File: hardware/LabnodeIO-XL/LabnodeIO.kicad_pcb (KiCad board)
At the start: 2 copper layers, 106 parts, among them J1 mc 0.5-2.5, J2 EXT3, U1 PCF8574, U2 PCA9685-TSSOP, U3 LM324, U4 LM324, U5 LM324, U6 LM324

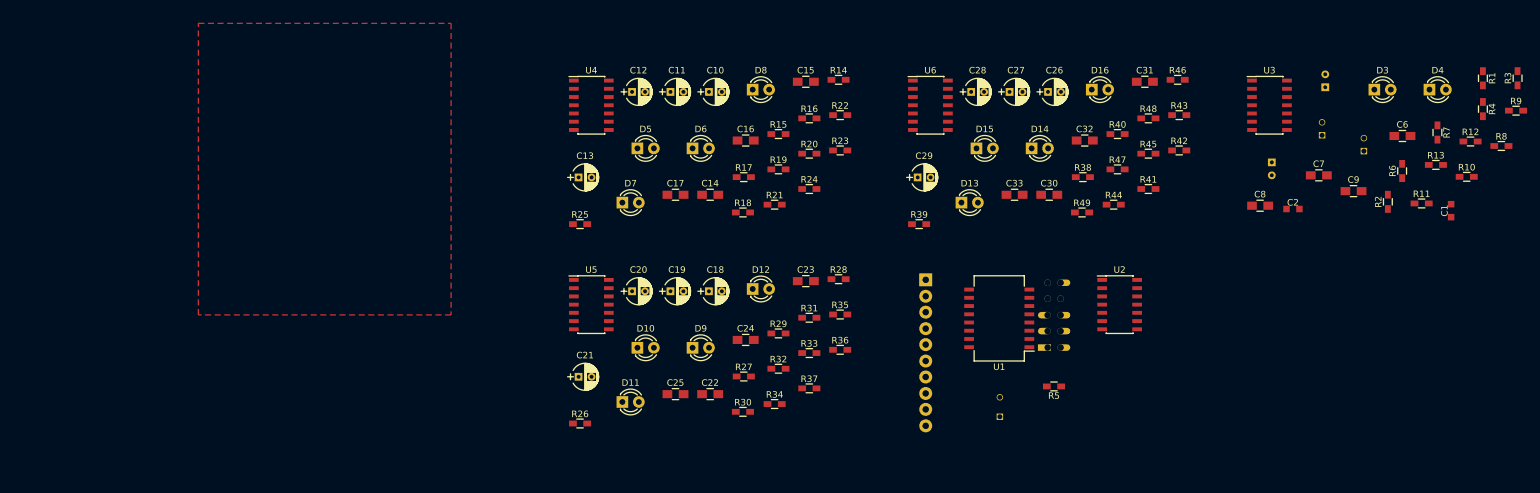
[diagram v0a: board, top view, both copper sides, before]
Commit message: Platinenlayout und 3d modell angefangen
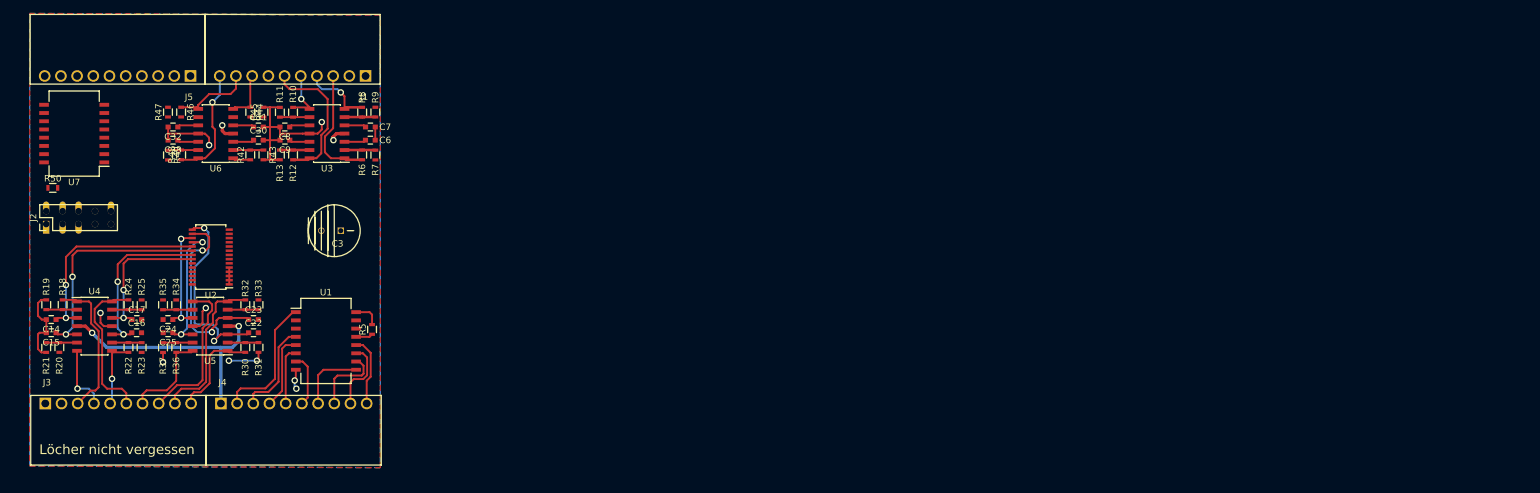
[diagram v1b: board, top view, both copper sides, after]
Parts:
- removed C1, C2: 100u, Capacitors_SMD:C_0805_HandSoldering
- removed C10, C11, C12, C13, C18, C19, C20, C21, C26, C27, C28, C29, C4, C5: 100u, Capacitors_THT:CP_Radial_D4.0mm_P2.00mm
- removed D1, D10, D11, D12, D13, D14, D15, D16, D2, D3, D4, D5, D6, D7, D8, D9: LED_Small, LEDs:LED_D3.0mm
- removed R1, R14, R15, R16, R17, R2, R26, R27, R28, R29, R3, R38, R39, R4, R40, R41: R, Resistors_SMD:R_0603_HandSoldering
- added J3: Conn_01x10, mc-0.5-2:MC-0,5-10-G-2,5, F.Cu at (16.4, 74.2)
- added J4: Conn_01x10, mc-0.5-2:MC-0,5-10-G-2,5, F.Cu at (43.5, 74.2)
- added J5: Conn_01x10, mc-0.5-2:MC-0,5-10-G-2,5, F.Cu at (38.8, 23.6)
- added R50: 1k5, Resistors_SMD:R_0603, F.Cu at (17.5, 40.9)
- added U7: PCF8574, Housings_SOIC:SOIC-16W_7.5x12.8mm_Pitch1.27mm, F.Cu at (20.8, 32.5)
- C14, C15, C16, C17, C22, C23, C24, C25, C30, C31, C32, C33, C6, C7, C8, C9: footprint Capacitors_SMD:C_0805_HandSoldering -> Capacitors_SMD:C_0603
- C3, J2: moved to F.Cu
- J1: value mc 0.5-2.5 -> Conn_01x10; footprint Connectors_Molex:Molex_KK-6410-10_10x2.54mm_Straight -> mc-0.5-2:MC-0,5-10-G-2,5; moved to F.Cu
- R10, R11, R12, R13, R18, R19, R20, R21, R22, R23, R24, R25, R30, R31, R32, R33, R34, R35, R36, R37, R42, R43, R44, R45, R46, R47, R48, R49, R5, R6, R7, R8, R9: footprint Resistors_SMD:R_0603_HandSoldering -> Resistors_SMD:R_0603
- U2: footprint Housings_SOIC:SOIC-14_3.9x8.7mm_Pitch1.27mm -> Housings_SSOP:TSSOP-28_4.4x9.7mm_Pitch0.65mm
- moved R12 181.7 mm to (54.6, 35.8), turned to 90 degrees
- moved R10 181.4 mm to (54.6, 29.2), turned to 270 degrees
- moved R13 178.4 mm to (52.6, 35.8), turned to 270 degrees
- moved R11 176.8 mm to (52.6, 29.2), turned to 90 degrees
- moved R9 176.0 mm to (67.3, 29.2), turned to 90 degrees
- moved R8 175.9 mm to (65.3, 29.2), turned to 270 degrees
- moved C9 165.1 mm to (53.4, 33.5), turned to 180 degrees
- moved R7 164.0 mm to (67.3, 35.8)
- moved R6 160.5 mm to (65.3, 35.8)
- moved C6 159.3 mm to (66.5, 33.5)
- moved J2 155.7 mm to (16.5, 46.5), turned to 90 degrees
- moved R46 153.9 mm to (37.3, 29.2), turned to 270 degrees
- moved C8 151.0 mm to (53.3, 31.5), turned to 180 degrees
- moved R48 149.4 mm to (37.3, 35.8), turned to 90 degrees
- moved R47 146.8 mm to (35.3, 29.2), turned to 90 degrees
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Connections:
- J1 pad 1: Net-(J1-Pad1) -> GND
- J1 pad 10: +12V -> /analog5-8/out4
- J1 pad 2: Net-(J1-Pad2) -> GND
- J1 pad 3: Net-(J1-Pad3) -> /analog1-4/out1
- J1 pad 4: Net-(J1-Pad4) -> /analog1-4/out2
- J1 pad 5: Net-(J1-Pad5) -> /analog1-4/out3
- J1 pad 6: Net-(J1-Pad6) -> /analog1-4/out4
- J1 pad 7: Net-(J1-Pad7) -> /analog5-8/out1
- J1 pad 8: Net-(J1-Pad8) -> /analog5-8/out2
- J1 pad 9: +5V -> /analog5-8/out3
- U1 pad 1: GND -> +5V
- U1 pad 10: Net-(J1-Pad3) -> /digital 1-8/digital6
- U1 pad 11: Net-(J1-Pad2) -> /digital 1-8/digital7
- U1 pad 12: Net-(J1-Pad1) -> /digital 1-8/digital8
- U1 pad 4: Net-(J1-Pad8) -> /digital 1-8/digital1
- U1 pad 5: Net-(J1-Pad7) -> /digital 1-8/digital2
- U1 pad 6: Net-(J1-Pad6) -> /digital 1-8/digital3
- U1 pad 7: Net-(J1-Pad5) -> /digital 1-8/digital4
- U1 pad 9: Net-(J1-Pad4) -> /digital 1-8/digital5
- U2 pad 1: (no net) -> GND
- U2 pad 10: /analog5-8/out1 -> /analog5-8/in1
- U2 pad 11: /analog5-8/out2 -> /analog5-8/in2
- U2 pad 12: /analog5-8/out3 -> /analog5-8/in3
- U2 pad 13: /analog5-8/out4 -> /analog5-8/in4
- U2 pad 2: (no net) -> GND
- U2 pad 3: (no net) -> GND
- U2 pad 4: (no net) -> GND
- U2 pad 5: (no net) -> GND
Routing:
- net GND: track 0.00 -> 76.6 mm, vias 0 -> 9
- net +12V: track 0.00 -> 44.7 mm, vias 0 -> 4
- net /analog9-12/in2: track 0.00 -> 34.7 mm, vias 0 -> 2
- net /analog9-12/in1: track 0.00 -> 32.9 mm, vias 0 -> 2
- net /analog13-16/in2: track 0.00 -> 29.7 mm, vias 0 -> 2
- net /analog13-16/in1: track 0.00 -> 29.6 mm, vias 0 -> 2
- net /analog9-12/in3: track 0.00 -> 26.4 mm, vias 0 -> 2
- net +5V: track 0.00 -> 24.5 mm
- net /analog13-16/out2: track 0.00 -> 24.5 mm
- net /analog9-12/out4: track 0.00 -> 23.8 mm
- net /analog13-16/out3: track 0.00 -> 23.8 mm
- net /analog9-12/out1: track 0.00 -> 22.7 mm
- net /analog9-12/in4: track 0.00 -> 22.5 mm, vias 0 -> 2
- net /analog1-4/out4: track 0.00 -> 22.4 mm
- net /analog13-16/in4: track 0.00 -> 20.9 mm, vias 0 -> 2
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- added copper zone on B.Cu, net GND
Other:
- net class Default: clearance 0.4 -> 0.25; trace_width 0.5 -> 0.3; via_dia 1.5 -> 1; via_drill 1 -> 0.6
- net class POWER added: clearance 0.25, trace_width 0.5, via_dia 1, via_drill 0.6
- rule trace_clearance: 0.4 -> 0.25
- board text added: "Löcher nicht vergessen"

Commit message: pwm chip geroutet
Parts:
- moved C3 23.4 mm to (38.6, 47.5)
- moved U2 15.8 mm to (57.7, 51.3)
- moved R50 7.98 mm to (16.3, 33.0), turned to 270 degrees
- moved C15 3.57 mm to (17.0, 66.8)
- moved C16 3.57 mm to (30.2, 66.8)
- moved C22 3.57 mm to (48.2, 66.8)
- moved C25 3.57 mm to (35.1, 66.8)
- moved R18 3.57 mm to (18.8, 62.5)
- moved R19 3.57 mm to (16.3, 62.5)
- moved R24 3.57 mm to (29.0, 62.5)
- moved R25 3.57 mm to (31.0, 62.5)
- moved R32 3.57 mm to (47.0, 62.5)
- moved R33 3.57 mm to (49.0, 62.5)
- moved R34 3.57 mm to (36.3, 62.5)
- moved R35 3.57 mm to (34.3, 62.5)
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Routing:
- net GND: track 76.6 -> 197.2 mm, vias 9 -> 23
- net /analog5-8/in3: track 3.25 -> 42.3 mm, vias 0 -> 2
- net /analog5-8/in4: track 3.25 -> 36.6 mm, vias 0 -> 2
- net +5V: track 24.5 -> 56.1 mm
- net /analog5-8/in2: track 3.25 -> 32.9 mm, vias 0 -> 2
- net /analog5-8/in1: track 3.25 -> 31.8 mm, vias 0 -> 2
- net +12V: track 44.7 -> 71.7 mm
- net /analog9-12/in3: track 26.4 -> 51.0 mm
- net /analog1-4/in3: track 3.17 -> 26.7 mm, vias 0 -> 2
- net /analog1-4/in2: track 3.35 -> 26.2 mm, vias 0 -> 2
- net /analog5-8/out1: track 2.73 -> 24.5 mm, vias 0 -> 1
- net /analog1-4/in1: track 3.34 -> 24.1 mm, vias 0 -> 2
- net /analog1-4/in4: track 3.15 -> 23.1 mm, vias 0 -> 2
- net /analog9-12/in1: track 32.9 -> 52.5 mm
- net /analog13-16/in3: track 17.1 -> 36.3 mm
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
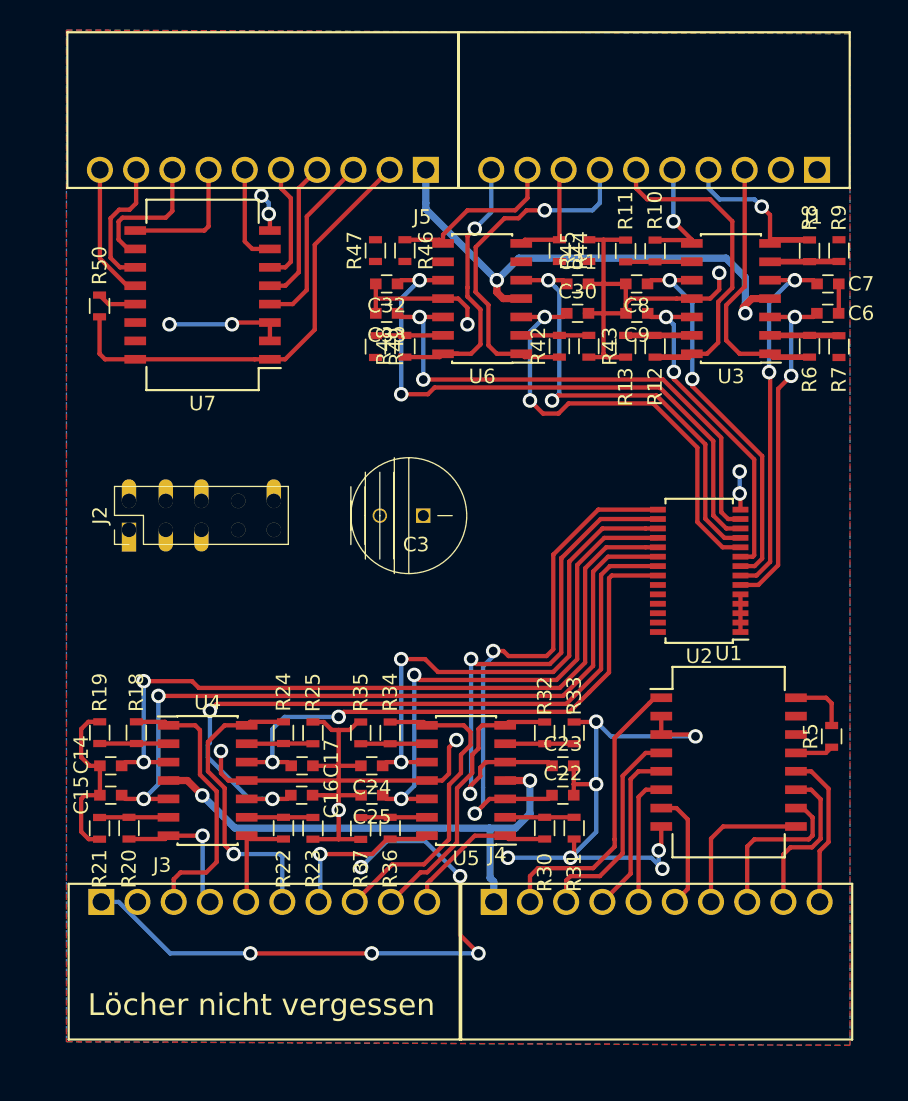
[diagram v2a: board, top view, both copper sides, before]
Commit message: eingangswiderstände hinzugefuegt und geroutet
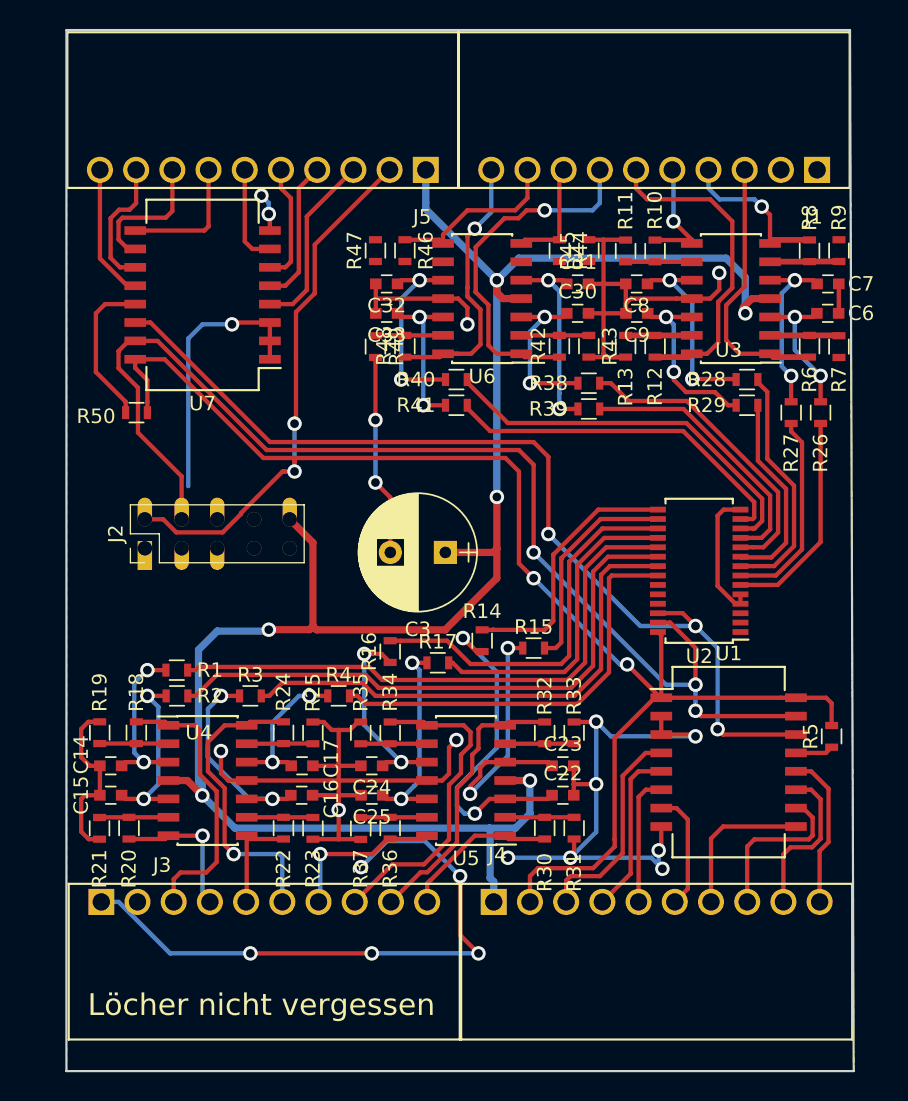
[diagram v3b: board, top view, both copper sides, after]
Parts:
- added R1: 22k, Resistors_SMD:R_0603, F.Cu at (21.6, 58.2)
- added R14: 22k, Resistors_SMD:R_0603, F.Cu at (42.7, 56.1)
- added R15: 22k, Resistors_SMD:R_0603, F.Cu at (46.2, 56.6)
- added R16: 22k, Resistors_SMD:R_0603, F.Cu at (36.3, 56.9)
- added R17: 22k, Resistors_SMD:R_0603, F.Cu at (39.6, 57.7)
- added R2: 22k, Resistors_SMD:R_0603, F.Cu at (21.6, 59.9)
- added R26: 22k, Resistors_SMD:R_0603, F.Cu at (66.0, 40.4)
- added R27: 22k, Resistors_SMD:R_0603, F.Cu at (64.0, 40.4)
- added R28: 22k, Resistors_SMD:R_0603, F.Cu at (61.0, 38.1)
- added R29: 22k, Resistors_SMD:R_0603, F.Cu at (61.0, 39.9)
- added R3: 22k, Resistors_SMD:R_0603, F.Cu at (26.7, 59.9)
- added R38: 22k, Resistors_SMD:R_0603, F.Cu at (50.0, 38.4)
- added R39: 22k, Resistors_SMD:R_0603, F.Cu at (50.0, 40.1)
- added R4: 22k, Resistors_SMD:R_0603, F.Cu at (32.8, 59.9)
- added R40: 22k, Resistors_SMD:R_0603, F.Cu at (40.9, 38.1)
- added R41: 22k, Resistors_SMD:R_0603, F.Cu at (40.9, 39.9)
- moved R50 7.80 mm to (18.8, 40.4), turned to 0 degrees
- moved C3 2.96 mm to (40.1, 50.0)
- moved J2 1.68 mm to (19.4, 49.8)
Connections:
- C14 pad 1: /analog9-12/in1 -> Net-(C14-Pad1)
- C15 pad 1: /analog9-12/in2 -> Net-(C15-Pad1)
- C16 pad 1: /analog9-12/in3 -> Net-(C16-Pad1)
- C17 pad 1: /analog9-12/in4 -> Net-(C17-Pad1)
- C22 pad 1: /analog13-16/in1 -> Net-(C22-Pad1)
- C23 pad 1: /analog13-16/in2 -> Net-(C23-Pad1)
- C24 pad 1: /analog13-16/in3 -> Net-(C24-Pad1)
- C25 pad 1: /analog13-16/in4 -> Net-(C25-Pad1)
- C30 pad 1: /analog5-8/in1 -> Net-(C30-Pad1)
- C31 pad 1: /analog5-8/in2 -> Net-(C31-Pad1)
- C32 pad 1: /analog5-8/in3 -> Net-(C32-Pad1)
- C33 pad 1: /analog5-8/in4 -> Net-(C33-Pad1)
- C6 pad 1: /analog1-4/in1 -> Net-(C6-Pad1)
- C7 pad 1: /analog1-4/in2 -> Net-(C7-Pad1)
- C8 pad 1: /analog1-4/in3 -> Net-(C8-Pad1)
- C9 pad 1: /analog1-4/in4 -> Net-(C9-Pad1)
- U3 pad 10: /analog1-4/in3 -> Net-(C8-Pad1)
- U3 pad 12: /analog1-4/in4 -> Net-(C9-Pad1)
- U3 pad 3: /analog1-4/in1 -> Net-(C6-Pad1)
- U3 pad 5: /analog1-4/in2 -> Net-(C7-Pad1)
- U4 pad 10: /analog9-12/in3 -> Net-(C16-Pad1)
- U4 pad 12: /analog9-12/in4 -> Net-(C17-Pad1)
- U4 pad 3: /analog9-12/in1 -> Net-(C14-Pad1)
- U4 pad 5: /analog9-12/in2 -> Net-(C15-Pad1)
- U5 pad 10: /analog13-16/in3 -> Net-(C24-Pad1)
- U5 pad 12: /analog13-16/in4 -> Net-(C25-Pad1)
- U5 pad 3: /analog13-16/in1 -> Net-(C22-Pad1)
- U5 pad 5: /analog13-16/in2 -> Net-(C23-Pad1)
- U6 pad 10: /analog5-8/in3 -> Net-(C32-Pad1)
- U6 pad 12: /analog5-8/in4 -> Net-(C33-Pad1)
- U6 pad 3: /analog5-8/in1 -> Net-(C30-Pad1)
- U6 pad 5: /analog5-8/in2 -> Net-(C31-Pad1)
- U7 pad 1: +5V -> GND
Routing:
- net SDA: track 0.00 -> 81.7 mm, vias 0 -> 3
- net +5V: track 56.1 -> 129.2 mm, vias 0 -> 4
- net SCL: track 0.00 -> 66.8 mm, vias 0 -> 3
- net +12V: track 71.7 -> 137.0 mm, vias 4 -> 6
- net GND: track 197.2 -> 225.7 mm, vias 23 -> 22
- net /analog13-16/in2: track 37.7 -> 15.0 mm, vias 2 -> 0
- net Net-(C22-Pad1): track 0.00 -> 22.7 mm, vias 0 -> 2
- net Net-(C23-Pad1): track 0.00 -> 19.6 mm, vias 0 -> 2
- net /analog13-16/in1: track 37.2 -> 18.3 mm, vias 2 -> 0
- net Net-(C16-Pad1): track 0.00 -> 15.6 mm, vias 0 -> 2
- net /analog9-12/in3: track 51.0 -> 35.7 mm, vias 2 -> 0
- net /analog5-8/in3: track 42.3 -> 27.1 mm, vias 2 -> 0
- net /analog13-16/in4: track 36.9 -> 22.4 mm, vias 2 -> 0
- net Net-(C25-Pad1): track 0.00 -> 14.3 mm, vias 0 -> 2
- net Net-(C31-Pad1): track 0.00 -> 14.1 mm, vias 0 -> 2
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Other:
- board outline added: 54.4 x 71.9 mm
